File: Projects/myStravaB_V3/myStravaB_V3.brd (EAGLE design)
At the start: 52.3 x 77.5 mm, 82 parts, among them IC1 TPS63051RMWT, IC2 BMD-340-A-R, Q2 BSS138BKW, T2 BC847, U1 FXOS8700CQR1, U2 MCP73831, Y3 32.768kHz

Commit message: Replaced barometer in strava V3
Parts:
- removed MS1: MS5637, MS5637:MS5637
- added C17: 0.1uF, SparkFun-Capacitors:0603
- added IC3: BME280, bosch-bme280:BME280
- added R5: 100k, rcl:R0603
- moved U$16 1.30 mm to (-15.8, 0.04)
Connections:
- new net N$3: R5.2, U$1.P$3
- net GND: now also C17.2, IC3.1, IC3.5, IC3.7; no longer MS1.GND
- net INV: now also R5.1; no longer U$1.P$3
- net SCL: now also IC3.4; no longer MS1.SCL
- net SDA: now also IC3.3; no longer MS1.SDA
- net VCC: now also C17.1, IC3.2, IC3.6, IC3.8; no longer MS1.VDD
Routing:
- net VCC: track 117.5 -> 124.5 mm
- net N$3: track 0.00 -> 4.29 mm
- net INV: track 20.6 -> 18.0 mm
- net SDA: track 98.5 -> 100.4 mm, vias 4 -> 5
- net SWDCLK: track 36.2 -> 37.9 mm
- net LS027_SCK: track 32.2 -> 33.5 mm
- net LS027_MO: track 32.7 -> 34.0 mm
- net EXTCOMM1: track 3.44 -> 4.76 mm
- net LS027_CS: track 31.2 -> 32.6 mm
- net EXTMODE1: track 3.02 -> 4.28 mm
- net DISP1: track 7.10 -> 8.37 mm
- net NEO_PIN: track 35.4 -> 36.3 mm
- net N$15: track 5.36 -> 4.86 mm
- net GND: vias 195 -> 201
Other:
- outline, holes or cut-outs redrawn

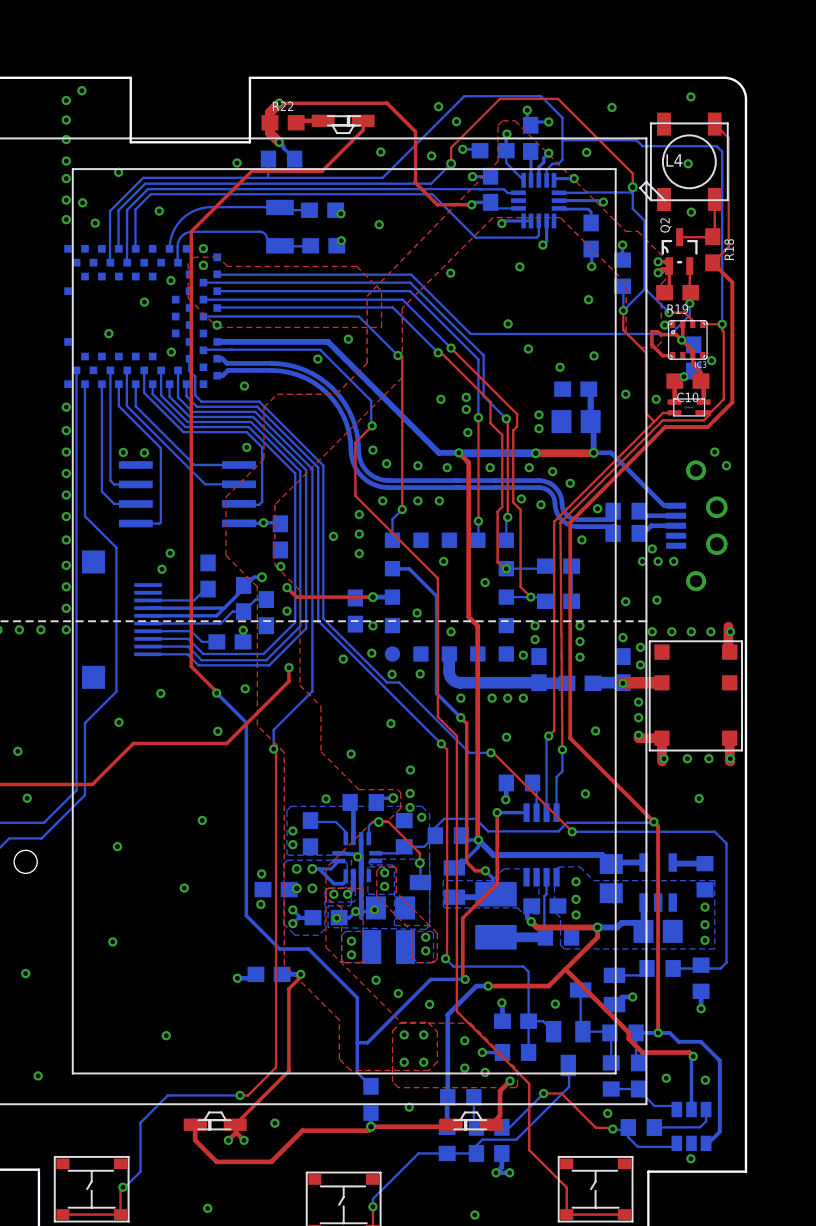
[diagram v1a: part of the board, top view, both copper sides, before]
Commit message: Corrected BMD340 footprint Update the board with FRAM, bme280 and new pins assignments
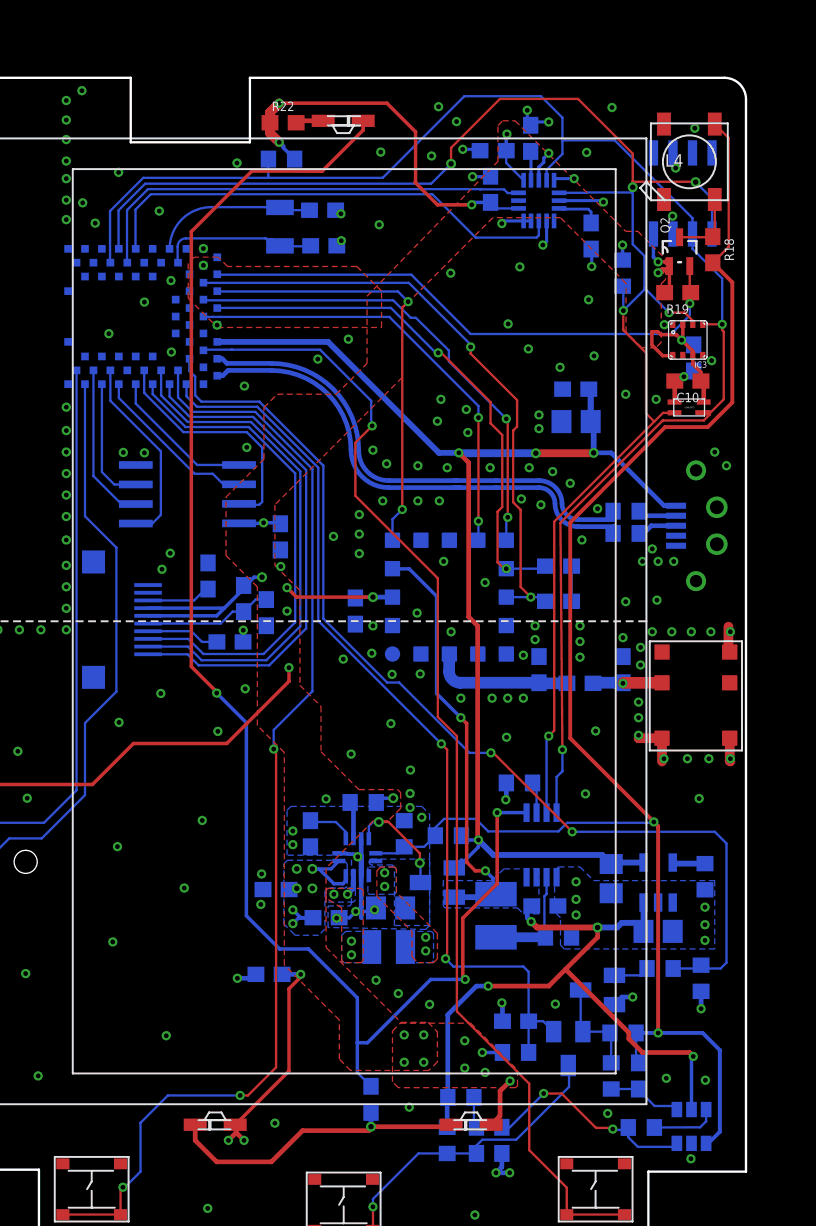
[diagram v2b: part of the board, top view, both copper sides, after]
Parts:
- added U3: (no value), FRAM:SOIC127P600X175-8N
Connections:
- net FIX: now also IC2.63; no longer IC2.23
- net GND: now also U3.2, U3.3, U3.4, U3.7
- net GPS_RST: now also IC2.19; no longer IC2.21
- net GPS_RX: now also IC2.21; no longer IC2.19
- net GPS_TX: now also IC2.23; no longer IC2.63
- net SCL: now also U3.6
- net SDA: now also U3.5
- net SPI_MI: now also IC2.42; no longer IC2.41
- net SPI_SCK: now also IC2.39; no longer IC2.38
- net SST_CS: now also IC2.40; no longer IC2.39
- net SST_WP: now also IC2.41; no longer IC2.40
- net VCC: now also U3.8
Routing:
- net SDA: track 100.4 -> 109.0 mm, vias 5 -> 6
- net SCL: track 104.4 -> 100.5 mm
- net FIX: track 26.2 -> 28.6 mm
- net VCC: track 124.5 -> 126.5 mm
- net GPS_RX: track 32.9 -> 31.3 mm
- net GPS_TX: track 30.6 -> 29.0 mm
- net GPS_RST: track 38.6 -> 39.9 mm
- net SPI_MI: track 9.53 -> 10.4 mm
- net SST_CS: track 11.8 -> 12.6 mm
- net SPI_SCK: track 11.7 -> 11.0 mm
- net SST_WP: track 8.93 -> 8.26 mm

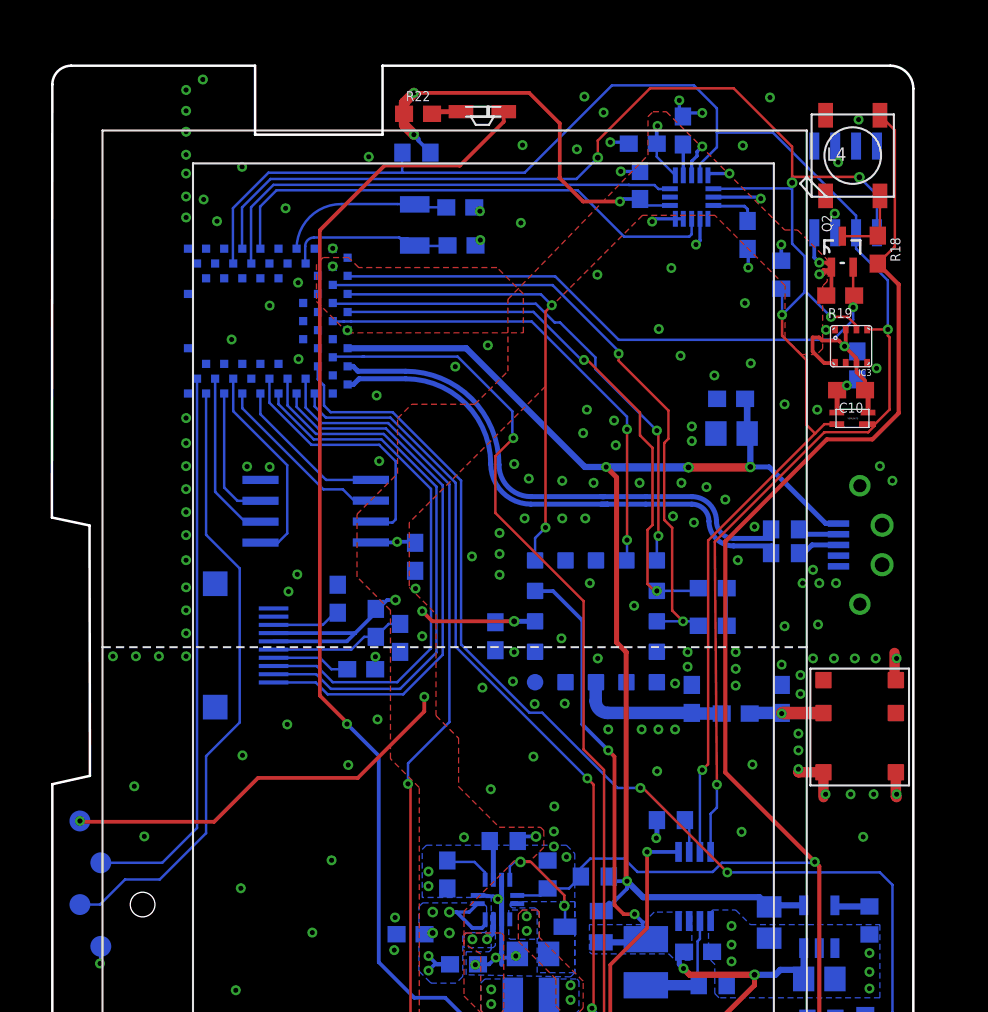
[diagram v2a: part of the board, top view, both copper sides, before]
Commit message: Thermal routing for BMD340
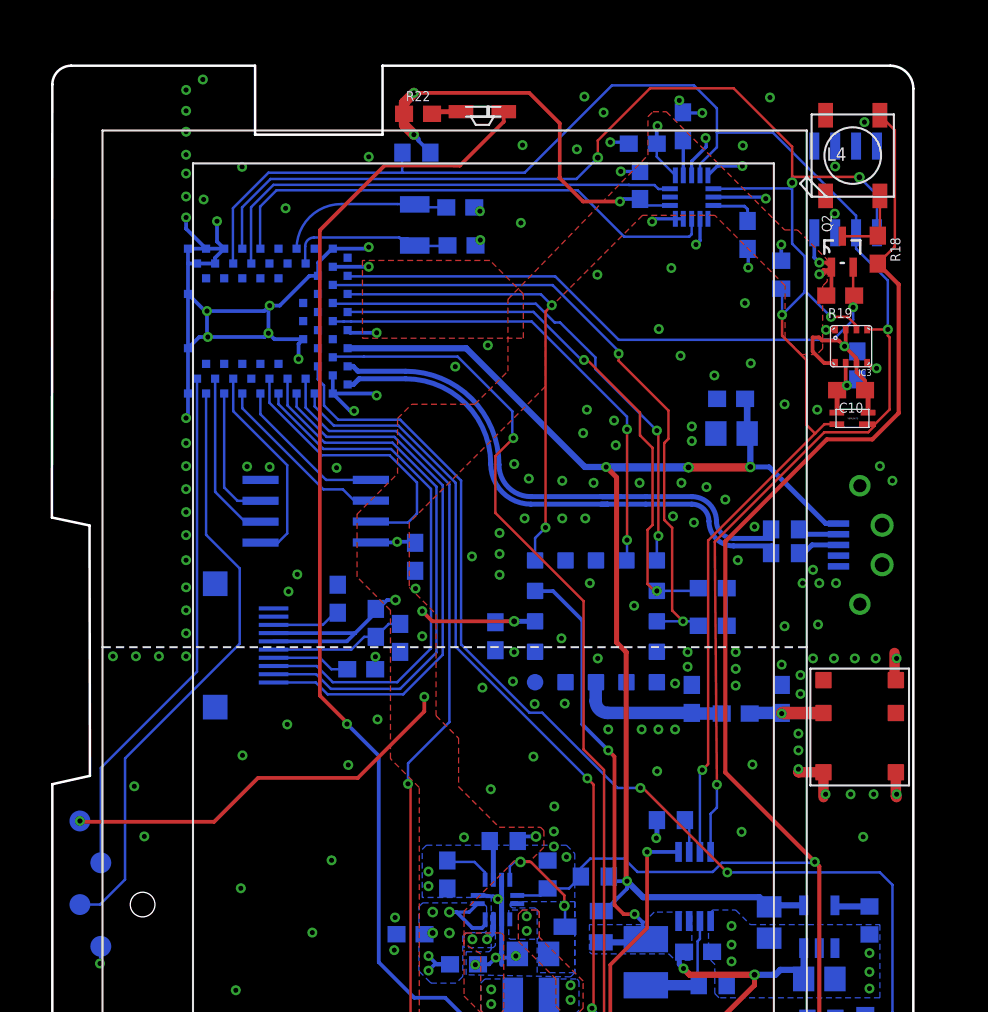
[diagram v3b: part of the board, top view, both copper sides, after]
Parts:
- BATT: value (none) -> 4.2V_LI-ION
- moved C6 0.25 mm to (12.2, 31.6)
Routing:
- net GND: track 48.1 -> 103.1 mm, vias 201 -> 203
- net VCC: track 126.5 -> 130.2 mm
- net SWDIO: track 34.0 -> 31.8 mm
- net USB_D0_N: track 30.9 -> 32.8 mm
- net SST_HOLD: track 15.8 -> 17.4 mm
- net SWDCLK: track 37.9 -> 36.6 mm
- net VUSB: track 80.2 -> 79.5 mm

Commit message: Thermals added
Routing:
- net GND: track 103.1 -> 116.4 mm, vias 203 -> 206
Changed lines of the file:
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@@
 <wire x1="1.143" y1="-18.5928" x2="1.143" y2="-19.304" width="0.3048" layer="16"/>
 <wire x1="21.5292" y1="14.2402" x2="21.5292" y2="15.5898" width="0.3048" layer="1"/>
-<polygon width="0.3048" layer="1" thermals="no" rank="6">
+<polygon width="0.3048" layer="1" rank="6">
 <vertex x="-35.687" y="50.927"/>
 <vertex x="41.783" y="50.927"/>
@@
 <wire x1="-5.627" y1="-22.86" x2="-5.640546875" y2="-22.926146875" width="0.3048" layer="16"/>
 <wire x1="-5.7014" y1="-22.987" x2="-5.640546875" y2="-22.926146875" width="0.3048" layer="16"/>
-<via x="-3.302" y="-14.5542" extent="1-16" drill="0.3048"/>
-<via x="-3.302" y="-13.6652" extent="1-16" drill="0.3048"/>
+<via x="-3.6068" y="-14.8336" extent="1-16" drill="0.3048"/>
+<via x="-3.6068" y="-13.9192" extent="1-16" drill="0.3048"/>
 <via x="5.08" y="-12.7762" extent="1-16" drill="0.3048"/>
 <via x="4.318" y="-12.1412" extent="1-16" drill="0.3048"/>
@@
 <wire x1="-23.2156" y1="-19.2024" x2="-23.2664" y2="-19.2532" width="0.2286" layer="16"/>
 <via x="22.5806" y="-34.9758" extent="1-16" drill="0.3048"/>
-<polygon width="0.3048" layer="16" thermals="no" rank="6">
+<polygon width="0.3048" layer="16" rank="6">
 <vertex x="-33.02" y="48.8442"/>
 <vertex x="44.45" y="48.8442"/>
@@
 <via x="0.9144" y="-15.3416" extent="1-16" drill="0.3048"/>
 <via x="2.0066" y="-18.796" extent="1-16" drill="0.3048"/>
-<via x="-0.4572" y="-19.3294" extent="1-16" drill="0.3048"/>
+<via x="-0.6604" y="-19.5326" extent="1-16" drill="0.3048"/>
 <via x="2.1082" y="-23.368" extent="1-16" drill="0.3048"/>
 <via x="5.588" y="-24.9428" extent="1-16" drill="0.3048"/>
@@
 <contactref element="C19" pad="2"/>
 <via x="8.0772" y="12.2428" extent="1-16" drill="0.3048"/>
-<via x="0.7874" y="-18.8976" extent="1-16" drill="0.3048"/>
-<wire x1="0.7874" y1="-18.8976" x2="0.8382" y2="-18.8976" width="0.2286" layer="16"/>
-<wire x1="0.8382" y1="-18.8976" x2="1.143" y2="-18.5928" width="0.2286" layer="16"/>
-<wire x1="-0.293" y1="-19.304" x2="0.381" y2="-19.304" width="0.2286" layer="16"/>
-<wire x1="0.381" y1="-19.304" x2="0.7874" y2="-18.8976" width="0.2286" layer="16"/>
-<wire x1="2.098" y1="-18.669" x2="1.8694" y2="-18.8976" width="0.2286" layer="16"/>
-<wire x1="1.8694" y1="-18.8976" x2="0.7874" y2="-18.8976" width="0.2286" layer="16"/>
+<via x="1.27" y="-18.8722" extent="1-16" drill="0.3048"/>
+<wire x1="1.143" y1="-18.5928" x2="1.143" y2="-18.7452" width="0.2286" layer="16"/>
+<wire x1="1.27" y1="-18.8722" x2="1.143" y2="-18.7452" width="0.2286" layer="16"/>
+<wire x1="-0.293" y1="-19.304" x2="0.8382" y2="-19.304" width="0.2286" layer="16"/>
+<wire x1="0.8382" y1="-19.304" x2="1.27" y2="-18.8722" width="0.2286" layer="16"/>
+<wire x1="2.098" y1="-18.669" x2="1.8948" y2="-18.8722" width="0.2286" layer="16"/>
+<wire x1="1.8948" y1="-18.8722" x2="1.27" y2="-18.8722" width="0.2286" layer="16"/>
 <contactref element="C44" pad="1"/>
 <via x="-5.334" y="-16.4592" extent="1-16" drill="0.3048"/>
@@
 <wire x1="22.0524" y1="17.2376" x2="22.0524" y2="15.946" width="0.2286" layer="1"/>
 <wire x1="22.0524" y1="15.946" x2="22.1234" y2="15.875" width="0.2286" layer="1"/>
+<via x="-17.907" y="19.812" extent="1-16" drill="0.3048"/>
+<wire x1="-12.7174" y1="2.3252" x2="-10.5294" y2="2.3252" width="0.254" layer="16"/>
+<wire x1="-10.5294" y1="2.3252" x2="-10.5156" y2="2.3114" width="0.254" layer="16"/>
+<wire x1="-10.5294" y1="2.3252" x2="-11.2776" y2="3.0734" width="0.254" layer="16"/>
+<wire x1="-11.2776" y1="3.0734" x2="-11.2776" y2="4.3942" width="0.254" layer="16"/>
+<wire x1="-12.7174" y1="1.8252" x2="-11.0294" y2="1.8252" width="0.254" layer="16"/>
+<wire x1="-11.0294" y1="1.8252" x2="-10.5294" y2="2.3252" width="0.254" layer="16"/>
+<wire x1="-12.7174" y1="2.3252" x2="-13.9838" y2="2.3252" width="0.254" layer="16"/>
+<wire x1="-13.9838" y1="2.3252" x2="-14.1986" y2="2.54" width="0.254" layer="16"/>
+<wire x1="-14.1986" y1="2.54" x2="-13.3858" y2="3.3528" width="0.254" layer="16"/>
+<wire x1="-13.3858" y1="3.3528" x2="-11.811" y2="3.3528" width="0.254" layer="16"/>
+<wire x1="-12.7174" y1="1.8252" x2="-14.1696" y2="1.8252" width="0.254" layer="16"/>
+<wire x1="-14.1696" y1="1.8252" x2="-14.1986" y2="1.8542" width="0.254" layer="16"/>
+<wire x1="-14.1986" y1="1.8542" x2="-14.1986" y2="2.54" width="0.254" layer="16"/>
+<via x="10.9982" y="-31.2928" extent="1-16" drill="0.3048"/>
+<via x="12.8778" y="-29.4132" extent="1-16" drill="0.3048"/>
 </signal>
 <signal name="SDA">
@@
 <vertex x="1.9304" y="-13.0048"/>
 <vertex x="-1.143" y="-16.0782"/>
-<vertex x="-1.143" y="-21.2344"/>
-<vertex x="3.7338" y="-26.1112"/>
+<vertex x="-1.143" y="-22.2504"/>
+<vertex x="2.7178" y="-26.1112"/>
 <vertex x="5.4864" y="-26.1112"/>
 <vertex x="6.096" y="-26.7208"/>
@@
 <wire x1="-3.556" y1="-3.048" x2="-3.556" y2="-3.937" width="0.2286" layer="1"/>
 <wire x1="-3.556" y1="-3.937" x2="-7.5946" y2="-7.9756" width="0.2286" layer="1"/>
-<wire x1="-7.052" y1="-32.766" x2="-3.556" y2="-29.27" width="0.2286" layer="1"/>
-<wire x1="-3.556" y1="-29.27" x2="-3.556" y2="-23.9268" width="0.2286" layer="1"/>
-<wire x1="-3.556" y1="-23.9268" x2="-2.794" y2="-23.1648" width="0.2286" layer="1"/>
+<wire x1="-7.052" y1="-32.766" x2="-3.8354" y2="-29.5494" width="0.2286" layer="1"/>
+<wire x1="-3.8354" y1="-29.5494" x2="-3.8354" y2="-24.2062" width="0.2286" layer="1"/>
+<wire x1="-3.8354" y1="-24.2062" x2="-2.794" y2="-23.1648" width="0.2286" layer="1"/>
 <wire x1="-2.794" y1="-23.1648" x2="-2.794" y2="-22.987" width="0.2286" layer="1"/>
 <wire x1="-3.9234" y1="30.8474" x2="-4.191" y2="31.115" width="0.3048" layer="16"/>
@@
 <contactref element="BTND1" pad="P$2"/>
 <wire x1="14.508" y1="-38.607" x2="18.258" y2="-38.607" width="0.1524" layer="1"/>
-<wire x1="7.366" y1="-7.493" x2="7.366" y2="-25.4" width="0.1524" layer="1"/>
-<wire x1="7.366" y1="-25.4" x2="12.065" y2="-30.099" width="0.1524" layer="1"/>
-<wire x1="12.065" y1="-30.099" x2="12.065" y2="-34.417" width="0.1524" layer="1"/>
+<wire x1="7.366" y1="-7.493" x2="7.366" y2="-24.892" width="0.1524" layer="1"/>
+<wire x1="7.366" y1="-24.892" x2="11.684" y2="-29.21" width="0.1524" layer="1"/>
+<wire x1="11.684" y1="-29.21" x2="11.684" y2="-34.036" width="0.1524" layer="1"/>
 <wire x1="14.508" y1="-36.86" x2="14.508" y2="-38.607" width="0.1524" layer="1"/>
-<wire x1="12.065" y1="-34.417" x2="14.508" y2="-36.86" width="0.1524" layer="1"/>
+<wire x1="11.684" y1="-34.036" x2="14.508" y2="-36.86" width="0.1524" layer="1"/>
 <wire x1="6.1214" y1="2.7686" x2="0.762" y2="8.128" width="0.1524" layer="1"/>
 <wire x1="6.1214" y1="2.7686" x2="6.1214" y2="-6.2484" width="0.1524" layer="1"/>
@@
 <wire x1="1.792821875" y1="12.735978125" x2="1.792821875" y2="14.303121875" width="0.1524" layer="16"/>
 <wire x1="1.792821875" y1="14.303121875" x2="-1.53165625" y2="17.6276" width="0.1524" layer="16"/>
-<wire x1="-1.53165625" y1="17.6276" x2="-7.234403125" y2="17.6276" width="0.1524" layer="16"/>
+<wire x1="-1.53165625" y1="17.6276" x2="-9.0776" y2="17.6276" width="0.1524" layer="16"/>
 <contactref element="IC2" pad="27"/>
-<wire x1="-7.234403125" y1="17.6276" x2="-9.0776" y2="17.6276" width="0.1524" layer="16"/>
 <wire x1="-9.1186" y1="17.5866" x2="-9.0776" y2="17.6276" width="0.1524" layer="16"/>
 </signal>
@@
 <wire x1="10.3124" y1="12.08274375" x2="10.3124" y2="7.39905625" width="0.1524" layer="1"/>
 <wire x1="9.5504" y1="14.224" x2="9.5504" y2="12.84474375" width="0.1524" layer="1"/>
-<wire x1="10.0076" y1="7.09425625" x2="10.0076" y2="3.81" width="0.1524" layer="1"/>
+<wire x1="10.0076" y1="7.09425625" x2="10.0076" y2="6.35" width="0.1524" layer="1"/>
 <wire x1="9.5504" y1="12.84474375" x2="10.3124" y2="12.08274375" width="0.1524" layer="1"/>
 <wire x1="10.3124" y1="7.39905625" x2="10.0076" y2="7.09425625" width="0.1524" layer="1"/>
-<wire x1="10.0076" y1="3.81" x2="10.4266" y2="3.391" width="0.1524" layer="1"/>
-<wire x1="10.4266" y1="3.391" x2="10.575" y2="3.391" width="0.1524" layer="1"/>
+<wire x1="10.575" y1="3.391" x2="10.575" y2="5.7826" width="0.1524" layer="1"/>
+<wire x1="10.575" y1="5.7826" x2="10.0076" y2="6.35" width="0.1524" layer="1"/>
 <via x="10.575" y="3.391" extent="1-16" drill="0.3048"/>
 <contactref element="IC2" pad="64"/>
@@
 <vertex x="1.27" y="-22.098"/>
 <vertex x="1.143" y="-22.225"/>
-<vertex x="0" y="-22.225"/>
-<vertex x="-0.127" y="-22.098"/>
+<vertex x="0.5334" y="-22.225"/>
+<vertex x="-0.127" y="-21.5646"/>
 <vertex x="-0.127" y="-18.669"/>
 </polygon>

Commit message: Strava V3 FRAM value set
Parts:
- U3: value (none) -> FM24CL16B
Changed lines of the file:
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@@
 <attribute name="VALUE" x="18.7198" y="-31.0388" size="1.27" layer="28" rot="MR180"/>
 </element>
-<element name="U3" library="FRAM" package="SOIC127P600X175-8N" value="" x="22.0472" y="27.7876" smashed="yes" rot="MR270">
+<element name="U3" library="FRAM" package="SOIC127P600X175-8N" value="FM24CL16B" x="22.0472" y="27.7876" smashed="yes" rot="MR270">
 <attribute name="NAME" x="18.73875" y="31.605040625" size="1.27248125" layer="26" rot="MR270"/>
 <attribute name="VALUE" x="26.496490625" y="31.60128125" size="1.27123125" layer="28" rot="MR270"/>
